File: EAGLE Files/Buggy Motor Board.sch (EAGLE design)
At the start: 63 parts, among them IC1 74LS595D, IC4 4050D, IC5 LP298XS, IC6 74LS595D, U1 MCP2551, X1 MICROSD, X2 5566-6, X3 5566-6, X4 5566-24, X5 5566-24, Y2 16MHZ

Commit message: Organization
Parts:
- removed ANALOG_IN: (no value), con-lstb:MA08-2
- removed C8: (no value), rcl:C-USC1210K
- removed X2, X3: 5566-6, con-molex:5566-6
- removed X4, X5: 5566-24, con-molex:5566-24
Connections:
- net +3V3: now also C3.1
- net +5V: no longer C3.1
- net AMUX_IN: no longer U$1.A7
- net CHAN0: no longer ANALOG_IN.16
- net CHAN1: no longer ANALOG_IN.15
- net CHAN10: no longer ANALOG_IN.6
- net CHAN11: no longer ANALOG_IN.5
- net CHAN12: no longer ANALOG_IN.4
- net CHAN13: no longer ANALOG_IN.3
- net CHAN14: no longer ANALOG_IN.2
- net CHAN15: no longer ANALOG_IN.1
- net CHAN2: no longer ANALOG_IN.14
- net CHAN3: no longer ANALOG_IN.13
- net CHAN4: no longer ANALOG_IN.12
- net CHAN5: no longer ANALOG_IN.11
- net CHAN6: no longer ANALOG_IN.10
- net CHAN7: no longer ANALOG_IN.9
- net CHAN8: no longer ANALOG_IN.8
- net CHAN9: no longer ANALOG_IN.7
- net GND: no longer C8.2
- net N$26: no longer C8.1
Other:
- note added: "Analog Input (Sensors)"
- moved on the sheet: ACT, C2, C3, C4, C5, C6, C7, DRIVER0, DRIVER1, IC4A, IC4B, IC4C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

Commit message: Tweak for Red Buggy
Removed IMU, second opto-coupler, shift registers;  added connectors for
Curtis motor controllers
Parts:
- removed C4, C5, C6, C7: (no value), SparkFun-Capacitors:CAP1206
- removed DRIVER0, DRIVER1: VN920, Wetmelon-DiscreteSemi:VN920
- removed IC1, IC6: 74LS595D, SparkFun-DigitalIC:74LS595D
- removed JMP1: 0R-JUMPA, jump-0r-smd:0R-JUMPA
- removed OK1: TIL199, optocoupler:TIL199
- removed R15, R16, R26, R27, R28, R6, R7: (no value), rcl:R-US_R1206
- removed R20, R21: 10k, adafruit:R-US_R0805
- removed R22, R23, R24, R25: 220, adafruit:R-US_R0805
- removed R29: 10k, rcl:R-US_R1206
- removed U2: (no value), SparkFun-Sensors:MPU-9150QFN-24-NP
- added JP1, JP5, JP6, JP7: M025MM, SparkFun-Connectors:M025MM
- added JP2: M023.5MM_LOCK, SparkFun-Connectors:M023.5MM_LOCK
- added JP3, JP4: (no value), SparkFun-Connectors:M03SCREW_LOCK
- added X2, X3: 5566-24, con-molex:5566-24
- added X4, X5: 5566-6, con-molex:5566-6
- R12, R13, R18, R19: value 220 -> 1k
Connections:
- removed net +36V: R1.2, R2.2, R26.2, R27.2, R28.2, R29.2, R3.2, R4.2
- removed net DAC2: U$4.VOUT
- removed net DOUT0: DRIVER0.OUTPUT
- removed net DOUT1: DRIVER1.OUTPUT
- removed net DRIVER0: DRIVER0.INPUT, IC1.QC
- removed net DRIVER1: DRIVER1.INPUT, IC1.QD
- removed net ESC: U2.E_SCL
- removed net ESD: U2.E_SDA
- removed net MPUCLKOUT: U2.CLKOUT
- removed net N$1: DRIVER0.CSENSE, R6.2
- removed net N$16: DRIVER1.CSENSE, R7.2
- removed net N$22: IC1.SCL, IC6.SCL, R15.1, U$1.D6*
- removed net N$24: IC6.SER, U$1.D4
- removed net N$25: IC1.SCK, IC6.SCK, U$1.D5*
- removed net N$26: IC1.RCK, IC6.RCK, U$1.D7
- removed net N$30: C4.1, U2.REGOUT
- removed net N$31: C5.1, U2.CPOUT
- removed net N$32: IC1.SER, IC6.QH*
- removed net N$33: OK1D.A, R25.1
- removed net N$34: JMP1-0R.2, U2.AD0
- removed net N$36: OK1A.A, R22.1
- removed net N$37: OK1B.A, R23.1
- removed net N$38: IC1.QE
- removed net N$39: IC1.QF
- removed net N$40: IC1.QG
- removed net N$41: IC1.QH
- removed net N$42: OK1C.A, R24.1
- removed net OOUT0: OK5A.COL, R1.1
- removed net OOUT1: OK5B.COL, R2.1
- removed net OOUT2: OK5C.COL, R3.1
- removed net OOUT3: OK5D.COL, R4.1
- removed net OOUT4: OK1A.COL, R26.1
- removed net OOUT5: OK1B.COL, R27.1
- removed net OOUT6: OK1C.COL, R28.1
- removed net OOUT7: OK1D.COL, R29.1
- removed net OPTO4: IC6.QE, R22.2
- removed net OPTO5: IC6.QF, R23.2
- removed net OPTO6: IC6.QG, R24.2
- removed net OPTO7: IC6.QH, R25.2
- new net CON0: JP5.1, X3-17.S
- new net CON1: JP6.1, X2-17.S
- new net DAC0: U$3.VOUT, X3-15.S
- new net FWD: OK5C.COL, R3.1, X2-10.S, X3-10.S
- new net ILOCK: JP7.1, X2-2.S, X3-2.S
- new net KSI: JP1.2, JP5.2, JP6.2, JP7.2, R1.2, R2.2, R3.2, R4.2, X2-1.S, X2-9.S, X3-1.S, X3-9.S
- new net MODE0: OK5A.COL, R1.1, X2-3.S, X3-3.S
- new net MODE1: OK5B.COL, R2.1, X2-4.S, X3-4.S
- new net REV: OK5D.COL, R4.1, X2-11.S, X3-11.S
- net +12V: now also JP2.2, R12.2, R13.2, R18.2, R19.2; no longer DRIVER0.VCC, DRIVER1.VCC
- net +3V3: no longer C6.1, C7.1, JMP1-0R.3, R20.2, R21.2, U2.VDD@13, U2.VDD@3, U2.VLOGIC
- net +5V: no longer IC6.VCC, R15.2, R16.1
- net AGND: now also JP1.1
- net CAN_CS: now also U$1.D10/SS*; no longer IC1.QB
- net DAC1: now also U$4.VOUT, X2-15.S; no longer U$3.VOUT
- net GND: now also JP2.1, JP3.1, JP4.1, X2-14.S, X3-14.S; no longer C4.2, C5.2, C6.2, C7.2, DRIVER0.GND, DRIVER1.GND, IC1.GND, IC6.GND, JMP1-0R.1, OK5A.C, OK5B.C, OK5C.C, OK5D.C, R6.1, R7.1, U2.CLKIN, U2.FSYNC, U2.GND@15, U2.GND@17, U2.GND@18
- net INT1: no longer U2.INT
- net N$28: no longer IC1.G, IC6.G, R16.2
- net OPTO0: now also JP3.3, OK5A.C; no longer IC6.QA, R12.2
- net OPTO1: now also JP3.2, OK5B.C; no longer IC6.QB, R13.2
- net OPTO2: now also JP4.3, OK5C.C; no longer IC6.QC, R18.2
- net OPTO3: now also JP4.2, OK5D.C; no longer IC6.QD, R19.2
- net SCL: no longer R21.1, U2.SCL
- net SDA: no longer R20.1, U2.SDA
- net SD_CS: now also U$1.D9*; no longer IC1.QA
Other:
- note added: "Controller Harness"
- note added: "Left Controller"
- note added: "Right Controller"
- moved on the sheet: ACT, C1, C2, C3, IC4A, IC4B, IC4C, IC4D, IC4E, IC4F, IC4P, IC5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

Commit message: Start Board, improve isolation
Started layout of board.  Changed Optocoupler.  Improved isolation by
moving DACs to the high voltage side and providing an isolated 5v rail.
Added Isolated I2C Converter to communicate with DACs across airgap.
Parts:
- removed JP1, JP5, JP6, JP7: M025MM, SparkFun-Connectors:M025MM
- removed JP2: M023.5MM_LOCK, SparkFun-Connectors:M023.5MM_LOCK
- removed JP3, JP4: (no value), SparkFun-Connectors:M03SCREW_LOCK
- removed OK5: TIL199, optocoupler:TIL199
- removed X4, X5: 5566-6, con-molex:5566-6
- added C4: (no value), rcl:C-USC1210K
- added CON0, CON1, ILOCK, KSI: M025MM, SparkFun-Connectors:M025MM
- added DIR, MODES: (no value), SparkFun-Connectors:M03SCREW_LOCK
- added PWR: M023.5MM_LOCK, SparkFun-Connectors:M023.5MM_LOCK
- added R15, R16: (no value), SparkFun-Resistors:RESISTOR0805-RES
- added R6, R7: 10k, SparkFun-Resistors:RESISTOR0805-RES
- added U$6: PS2801C-4, Wetmelon-DiscreteSemi:PS2801C-4
- added U$7: ADUM1251, Wetmelon-DigitalIC:ADUM1251
- added U$9: REE-0505S, Wetmelon-PowerIC:REE-0505S
- R1, R10, R11, R17, R2, R3, R4, R5, R8, R9: device rcl:R-US_R1206 -> SparkFun-Resistors:RESISTOR0805-RES
- R12, R13: value 1k -> 10k; device adafruit:R-US_R0805 -> SparkFun-Resistors:RESISTOR0805-RES
- R14: device adafruit:R-US_R0805 -> SparkFun-Resistors:RESISTOR0805-RES
- R18, R19: value 1k -> (none); device adafruit:R-US_R0805 -> SparkFun-Resistors:RESISTOR0805-RES
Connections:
- new net +5V/1: C4.1, R18.2, R19.2, R9.1, U$3.VDD, U$4.VDD, U$7.VDD2, U$9.VOUT
- new net GND1: C4.2, R8.1, U$3.VSS, U$4.VSS, U$7.GND2, U$9.GND2, X2-14.S, X3-14.S
- new net N$1: U$1.3V3
- new net SCL2: R19.1, U$3.SCL, U$4.SCL, U$7.SCL2
- new net SDA2: R18.1, U$3.SDA, U$4.SDA, U$7.SDA2
- net +12V: now also PWR.2, R6.2, R7.2; no longer JP2.2, R18.2, R19.2
- net +3V3: no longer U$1.3V3
- net +5V: now also R15.2, R16.2, U$7.VDD1, U$9.VIN; no longer R8.1, U$3.VDD, U$4.VDD
- net AGND: now also KSI.1, U$6G$1.L2, U$6G$2.L2, U$6G$3.L2, U$6G$4.L2; no longer JP1.1, OK5A.EMI, OK5B.EMI, OK5C.EMI, OK5D.EMI
- net CON0: now also CON0.1; no longer JP5.1
- net CON1: now also CON1.1; no longer JP6.1
- net FWD: now also R2.1, U$6G$2.L1; no longer OK5C.COL, R3.1
- net GND: now also DIR.1, MODES.1, PWR.1, U$7.GND1, U$9.GND1; no longer JP2.1, JP3.1, JP4.1, R9.1, U$3.VSS, U$4.VSS, X2-14.S, X3-14.S
- net ILOCK: now also ILOCK.1; no longer JP7.1
- net KSI: now also CON0.2, CON1.2, ILOCK.2, KSI.2; no longer JP1.2, JP5.2, JP6.2, JP7.2
- net MODE0: now also R4.1, U$6G$4.L1; no longer OK5A.COL, R1.1
- net MODE1: now also R3.1, U$6G$3.L1; no longer OK5B.COL, R2.1
- net N$12: now also R6.1, U$6G$1.A; no longer OK5A.A, R12.1
- net N$15: now also R7.1, U$6G$2.A; no longer OK5B.A, R13.1
- net N$27: now also R12.1, U$6G$3.A; no longer OK5C.A, R18.1
- net N$29: now also R13.1, U$6G$4.A; no longer OK5D.A, R19.1
- net OPTO0: now also MODES.3, U$6G$1.C; no longer JP3.3, OK5A.C
- net OPTO1: now also MODES.2, U$6G$2.C; no longer JP3.2, OK5B.C
- net OPTO2: now also DIR.3, U$6G$3.C; no longer JP4.3, OK5C.C
- net OPTO3: now also DIR.2, U$6G$4.C; no longer JP4.2, OK5D.C
- net REV: now also R1.1, U$6G$1.L1; no longer OK5D.COL, R4.1
- net SCL: now also R16.1, U$7.SCL1; no longer U$3.SCL, U$4.SCL
- net SDA: now also R15.1, U$7.SDA1; no longer U$3.SDA, U$4.SDA
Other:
- note added: "GLV Side"
- note added: "High Voltage Side (Max 48VDC Nominal)"
- moved on the sheet: C1, R1, R10, R11, R12, R13, R17, R18, R19, R2, R3, R4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

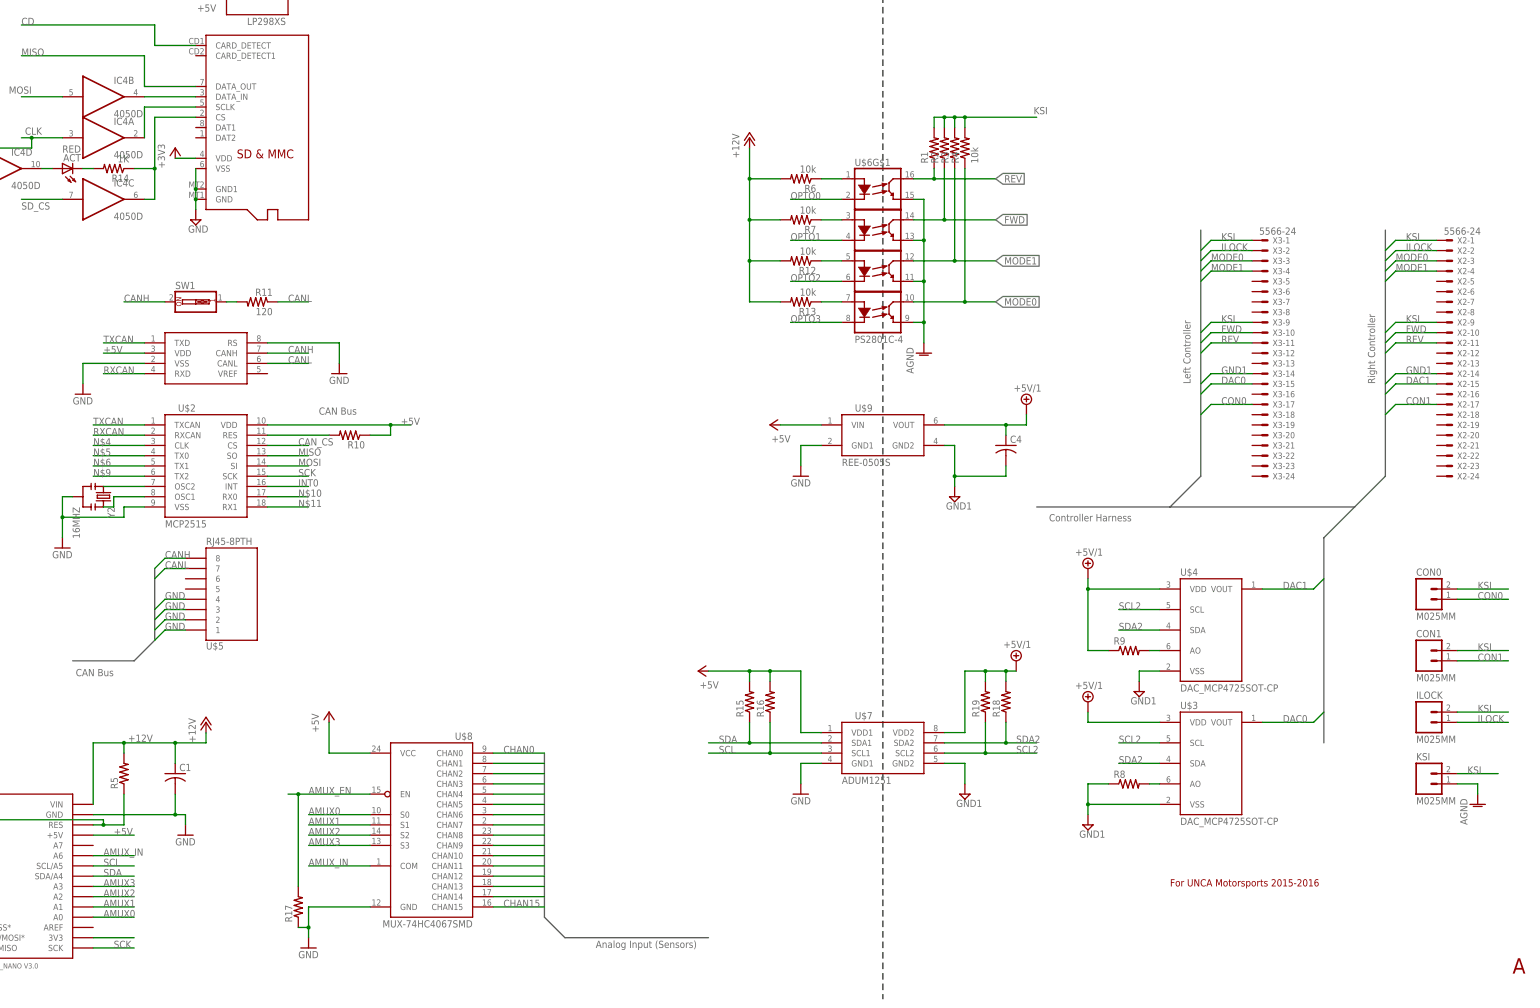
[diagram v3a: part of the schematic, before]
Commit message: Power consumption, analog input connectors
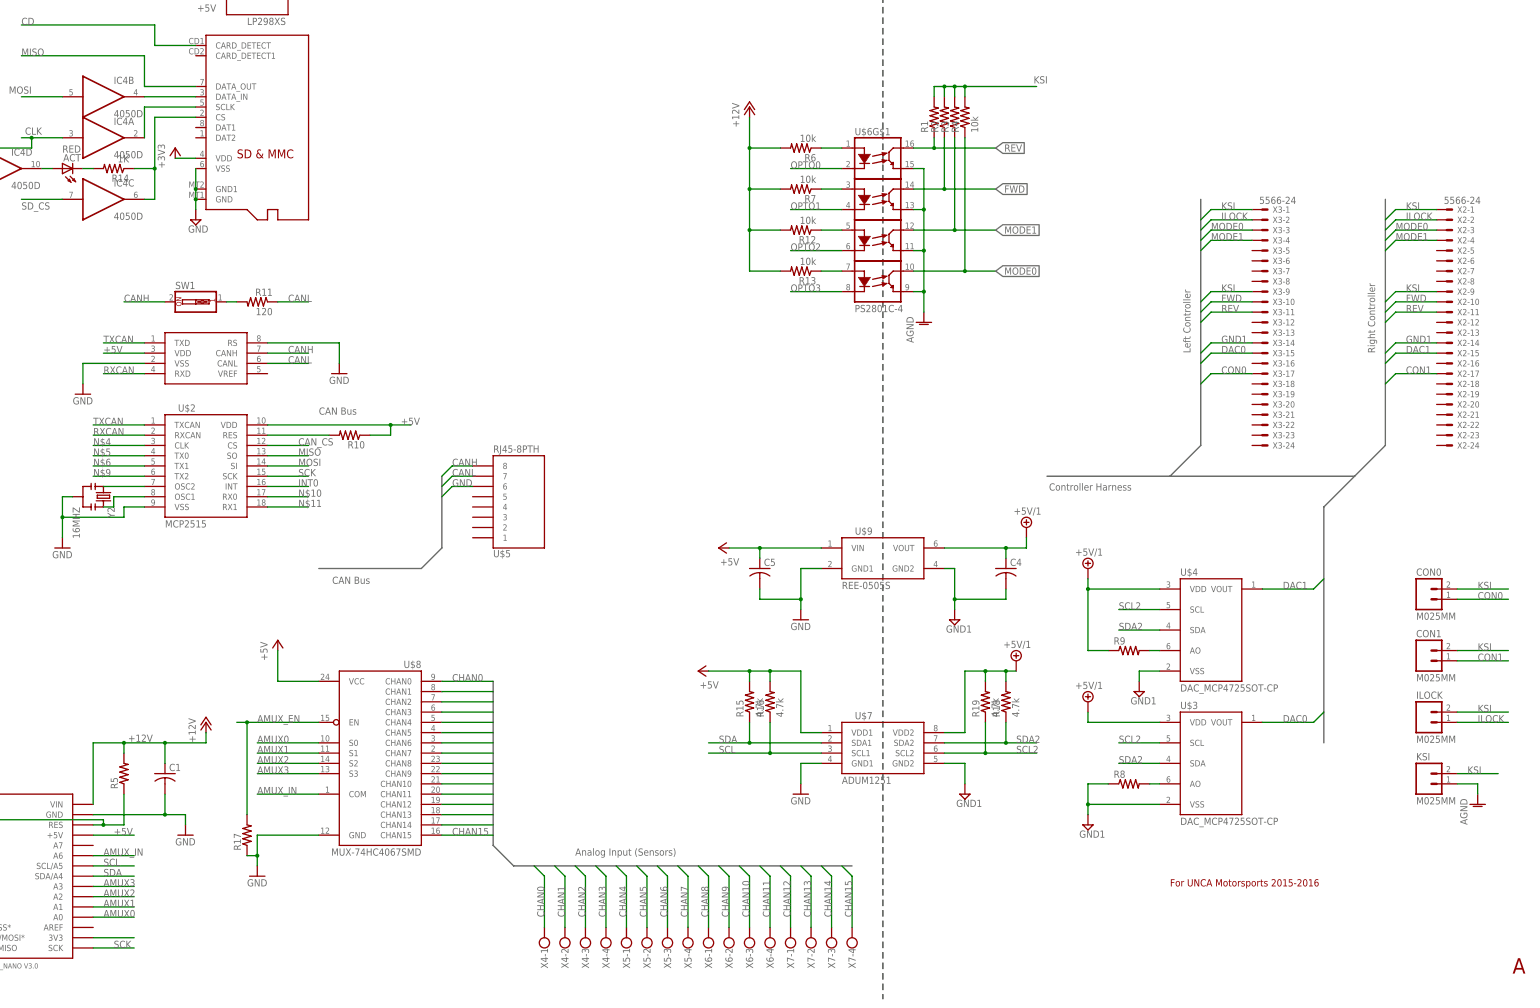
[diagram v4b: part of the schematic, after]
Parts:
- added C5: (no value), rcl:C-USC1210K
- added X4, X5, X6, X7: (no value), con-wago-500:W237-4
- R15, R16, R18, R19: value (none) -> 4.7k
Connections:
- net +5V: now also C5.1
- net CHAN0: now also X4-1.KL
- net CHAN1: now also X4-2.KL
- net CHAN10: now also X6-3.KL
- net CHAN11: now also X6-4.KL
- net CHAN12: now also X7-1.KL
- net CHAN13: now also X7-2.KL
- net CHAN14: now also X7-3.KL
- net CHAN15: now also X7-4.KL
- net CHAN2: now also X4-3.KL
- net CHAN3: now also X4-4.KL
- net CHAN4: now also X5-1.KL
- net CHAN5: now also X5-2.KL
- net CHAN6: now also X5-3.KL
- net CHAN7: now also X5-4.KL
- net CHAN8: now also X6-1.KL
- net CHAN9: now also X6-2.KL
- net GND: now also C5.2, U$5.6; no longer U$5.1, U$5.2, U$5.3, U$5.4
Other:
- moved on the sheet: C1, C4, R1, R12, R13, R17, R2, R3, R4, R6, R7, U$5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
